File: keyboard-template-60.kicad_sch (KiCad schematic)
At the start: 171 parts

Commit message: Part annotations
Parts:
- removed MX? (x8): MX-NoLED, symbol MX_Alps_Hybrid:MX-NoLED
- added MX? (x8): MX-NoLED, symbol MX_Alps_Hybrid:MX-NoLED
- gave numbers to parts that had none: 163
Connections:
- net COL10: now also MX?.1 (COL)
- net COL11: now also MX?.1 (COL)
- net COL12: now also MX?.1 (COL)
- net COL2: now also MX?.1 (COL)
- net COL3: now also MX?.1 (COL)
- net COL4: now also MX?.1 (COL)
- net COL6: now also MX?.1 (COL)
- net COL8: now also MX?.1 (COL)
- net at D63.2 (A): now also MX?.2 (ROW)
- net at D72.2 (A): now also MX?.2 (ROW)
- net at D37.2 (A): now also MX?.2 (ROW)
- net at D73.2 (A): now also MX?.2 (ROW)
- net at D39.2 (A): now also MX?.2 (ROW)
- net at D65.2 (A): now also MX?.2 (ROW)
- net at D71.2 (A): now also MX?.2 (ROW)
- net at D64.2 (A): now also MX?.2 (ROW)

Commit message: Update annotations
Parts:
- removed MX?: MX-NoLED, symbol MX_Alps_Hybrid:MX-NoLED
- added MX38-2: MX-NoLED, symbol MX_Alps_Hybrid:MX-NoLED
- gave numbers to parts that had none: 7
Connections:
- net COL6: now also MX38-2.1 (COL)
- net at D37.2 (A): now also MX38-2.2 (ROW)
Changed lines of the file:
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@@
   (junction (at 107.95 166.37) (diameter 0) (color 0 0 0 0)
   )
+  (junction (at 133.35 137.16) (diameter 0) (color 0 0 0 0)
+  )
   (junction (at 121.92 147.32) (diameter 0) (color 0 0 0 0)
   )
@@
   (junction (at 64.77 223.52) (diameter 0) (color 0 0 0 0)
   )
-  (junction (at 133.35 137.16) (diameter 0) (color 0 0 0 0)
-  )
   (junction (at 133.35 166.37) (diameter 0) (color 0 0 0 0)
   )
@@
     (stroke (width 0) (type default) (color 0 0 0 0))
   )
+  (wire (pts (xy 133.35 128.27) (xy 133.35 137.16))
+    (stroke (width 0) (type default) (color 0 0 0 0))
+  )
   (wire (pts (xy 294.64 177.8) (xy 304.8 177.8))
     (stroke (width 0) (type default) (color 0 0 0 0))
@@
     (stroke (width 0) (type default) (color 0 0 0 0))
   )
+  (wire (pts (xy 133.35 137.16) (xy 133.35 166.37))
+    (stroke (width 0) (type default) (color 0 0 0 0))
+  )
   (wire (pts (xy 115.57 176.53) (xy 128.27 176.53))
     (stroke (width 0) (type default) (color 0 0 0 0))
@@
     (stroke (width 0) (type default) (color 0 0 0 0))
   )
-  (wire (pts (xy 133.35 137.16) (xy 133.35 166.37))
-    (stroke (width 0) (type default) (color 0 0 0 0))
-  )
   (wire (pts (xy 96.52 223.52) (xy 102.87 223.52))
     (stroke (width 0) (type default) (color 0 0 0 0))
@@
     (stroke (width 0) (type default) (color 0 0 0 0))
   )
-  (wire (pts (xy 133.35 128.27) (xy 133.35 137.16))
-    (stroke (width 0) (type default) (color 0 0 0 0))
-  )
   (wire (pts (xy 171.45 52.07) (xy 171.45 90.17))
     (stroke (width 0) (type default) (color 0 0 0 0))
@@
   (symbol (lib_id "MX_Alps_Hybrid:MX-NoLED") (at 193.04 214.63 0) (unit 1)
     (in_bom yes) (on_board yes) (fields_autoplaced)
-    (property "Reference" "MX?" (id 0) (at 193.9256 208.28 0)
+    (property "Reference" "MX72-2" (id 0) (at 193.9256 208.28 0)
       (effects (font (size 1.524 1.524)))
     )
@@
   (symbol (lib_id "MX_Alps_Hybrid:MX-NoLED") (at 78.74 214.63 0) (unit 1)
     (in_bom yes) (on_board yes) (fields_autoplaced)
-    (property "Reference" "MX?" (id 0) (at 79.6256 208.28 0)
+    (property "Reference" "MX63-2" (id 0) (at 79.6256 208.28 0)
       (effects (font (size 1.524 1.524)))
     )
@@
     (pin "2")
   )
-  (symbol (lib_id "MX_Alps_Hybrid:MX-NoLED") (at 129.54 138.43 0) (unit 1)
-    (in_bom yes) (on_board yes) (fields_autoplaced)
-    (property "Reference" "MX?" (id 0) (at 130.4256 132.08 0)
-      (effects (font (size 1.524 1.524)))
-    )
-    (property "Value" "MX-NoLED" (id 1) (at 130.4256 133.35 0)
-      (effects (font (size 0.508 0.508)))
-    )
-    (property "Footprint" "" (id 2) (at 113.665 139.065 0)
-      (effects (font (size 1.524 1.524)) hide)
-    )
-    (property "Datasheet" "" (id 3) (at 113.665 139.065 0)
-      (effects (font (size 1.524 1.524)) hide)
-    )
-    (pin "1")
-    (pin "2")
-  )
   (symbol (lib_id "MX_Alps_Hybrid:MX-NoLED") (at 104.14 53.34 0) (unit 1)
     (in_bom yes) (on_board yes) (fields_autoplaced)
@@
   (symbol (lib_id "MX_Alps_Hybrid:MX-NoLED") (at 205.74 214.63 0) (unit 1)
     (in_bom yes) (on_board yes) (fields_autoplaced)
-    (property "Reference" "MX?" (id 0) (at 206.6256 208.28 0)
+    (property "Reference" "MX73-2" (id 0) (at 206.6256 208.28 0)
       (effects (font (size 1.524 1.524)))
     )
@@
   (symbol (lib_id "MX_Alps_Hybrid:MX-NoLED") (at 104.14 214.63 0) (unit 1)
     (in_bom yes) (on_board yes) (fields_autoplaced)
-    (property "Reference" "MX?" (id 0) (at 105.0256 208.28 0)
+    (property "Reference" "MX65-2" (id 0) (at 105.0256 208.28 0)
       (effects (font (size 1.524 1.524)))
     )
@@
   (symbol (lib_id "MX_Alps_Hybrid:MX-NoLED") (at 91.44 214.63 0) (unit 1)
     (in_bom yes) (on_board yes) (fields_autoplaced)
-    (property "Reference" "MX?" (id 0) (at 92.3256 208.28 0)
+    (property "Reference" "MX64-2" (id 0) (at 92.3256 208.28 0)
       (effects (font (size 1.524 1.524)))
     )
@@
   (symbol (lib_id "MX_Alps_Hybrid:MX-NoLED") (at 154.94 138.43 0) (unit 1)
     (in_bom yes) (on_board yes) (fields_autoplaced)
-    (property "Reference" "MX?" (id 0) (at 155.8256 132.08 0)
+    (property "Reference" "MX39-2" (id 0) (at 155.8256 132.08 0)
       (effects (font (size 1.524 1.524)))
     )
@@
   (symbol (lib_id "MX_Alps_Hybrid:MX-NoLED") (at 180.34 214.63 0) (unit 1)
     (in_bom yes) (on_board yes) (fields_autoplaced)
-    (property "Reference" "MX?" (id 0) (at 181.2256 208.28 0)
+    (property "Reference" "MX71-2" (id 0) (at 181.2256 208.28 0)
       (effects (font (size 1.524 1.524)))
     )
@@
     (pin "2")
   )
+  (symbol (lib_id "MX_Alps_Hybrid:MX-NoLED") (at 129.54 138.43 0) (unit 1)
+    (in_bom yes) (on_board yes) (fields_autoplaced)
+    (property "Reference" "MX38-2" (id 0) (at 130.4256 132.08 0)
+      (effects (font (size 1.524 1.524)))
+    )
+    (property "Value" "MX-NoLED" (id 1) (at 130.4256 133.35 0)
+      (effects (font (size 0.508 0.508)))
+    )
+    (property "Footprint" "" (id 2) (at 113.665 139.065 0)
+      (effects (font (size 1.524 1.524)) hide)
+    )
+    (property "Datasheet" "" (id 3) (at 113.665 139.065 0)
+      (effects (font (size 1.524 1.524)) hide)
+    )
+    (pin "1")
+    (pin "2")
+  )
   (symbol (lib_id "MX_Alps_Hybrid:MX-NoLED") (at 91.44 129.54 0) (unit 1)
     (in_bom yes) (on_board yes) (fields_autoplaced)
@@
       (reference "MX38") (unit 1) (value "MX-NoLED") (footprint "")
     )
+    (path "/f5c00a1c-6009-46f7-bb45-59e86d627cba"
+      (reference "MX38-2") (unit 1) (value "MX-NoLED") (footprint "")
+    )
     (path "/75294b3a-bcf4-4dee-b1b0-009fd10bd357"
       (reference "MX39") (unit 1) (value "MX-NoLED") (footprint "")
     )
+    (path "/a8b3e0bc-cfe9-4e81-954e-c1b4323435ec"
+      (reference "MX39-2") (unit 1) (value "MX-NoLED") (footprint "")
+    )
     (path "/f1689421-be27-441f-a091-cda9d302f953"
       (reference "MX40") (unit 1) (value "MX-NoLED") (footprint "")
@@
       (reference "MX63") (unit 1) (value "MX-NoLED") (footprint "")
     )
+    (path "/482255ed-4646-4a5e-9984-9a49bd9bd2b6"
+      (reference "MX63-2") (unit 1) (value "MX-NoLED") (footprint "")
+    )
     (path "/257a1eb5-8b33-4e19-9433-ae3ccc490c1b"
       (reference "MX64") (unit 1) (value "MX-NoLED") (footprint "")
     )
+    (path "/a11053e4-9eea-4e3c-beb1-319c66cc54d2"
+      (reference "MX64-2") (unit 1) (value "MX-NoLED") (footprint "")
+    )
     (path "/f2b5c4c7-e8e3-425d-a843-998f7557575d"
       (reference "MX65") (unit 1) (value "MX-NoLED") (footprint "")
     )
+    (path "/9dd9038e-364d-4f87-8675-edd37afc5560"
+      (reference "MX65-2") (unit 1) (value "MX-NoLED") (footprint "")
+    )
     (path "/aa9bb9c5-7107-46ce-943c-1c67b0dac064"
       (reference "MX67") (unit 1) (value "MX-NoLED") (footprint "")
@@
       (reference "MX71") (unit 1) (value "MX-NoLED") (footprint "")
     )
+    (path "/cc00687e-3426-4703-8265-70584ca7426c"
+      (reference "MX71-2") (unit 1) (value "MX-NoLED") (footprint "")
+    )
     (path "/a5e39449-0e3c-481c-85ad-81aa53ee1534"
       (reference "MX72") (unit 1) (value "MX-NoLED") (footprint "")
     )
+    (path "/17ef84ae-2695-4724-93fa-2a883f22ddd9"
+      (reference "MX72-2") (unit 1) (value "MX-NoLED") (footprint "")
+    )
     (path "/7db44cd6-4b9c-480e-9b0e-1b044e3ad474"
       (reference "MX73") (unit 1) (value "MX-NoLED") (footprint "")
     )
+    (path "/8d6e9efb-fed1-4560-b688-d3f05d3f7096"
+      (reference "MX73-2") (unit 1) (value "MX-NoLED") (footprint "")
+    )
     (path "/51589e35-00f2-4091-89f7-be519ee6b00c"
       (reference "MX74") (unit 1) (value "MX-NoLED") (footprint "")
@@
       (reference "MX75") (unit 1) (value "MX-NoLED") (footprint "")
     )
-    (path "/17ef84ae-2695-4724-93fa-2a883f22ddd9"
-      (reference "MX?") (unit 1) (value "MX-NoLED") (footprint "")
-    )
-    (path "/482255ed-4646-4a5e-9984-9a49bd9bd2b6"
-      (reference "MX?") (unit 1) (value "MX-NoLED") (footprint "")
-    )
-    (path "/6bff14b7-7fa8-49c6-9d76-d7cb980abe95"
-      (reference "MX?") (unit 1) (value "MX-NoLED") (footprint "")
-    )
-    (path "/8d6e9efb-fed1-4560-b688-d3f05d3f7096"
-      (reference "MX?") (unit 1) (value "MX-NoLED") (footprint "")
-    )
-    (path "/9dd9038e-364d-4f87-8675-edd37afc5560"
-      (reference "MX?") (unit 1) (value "MX-NoLED") (footprint "")
-    )
-    (path "/a11053e4-9eea-4e3c-beb1-319c66cc54d2"
-      (reference "MX?") (unit 1) (value "MX-NoLED") (footprint "")
-    )
-    (path "/a8b3e0bc-cfe9-4e81-954e-c1b4323435ec"
-      (reference "MX?") (unit 1) (value "MX-NoLED") (footprint "")
-    )
-    (path "/cc00687e-3426-4703-8265-70584ca7426c"
-      (reference "MX?") (unit 1) (value "MX-NoLED") (footprint "")
-    )
     (path "/decb3101-6255-4ab9-8fbc-5a7cad6b1f9e"

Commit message: Add power flag
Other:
- moved on the sheet: C4, C5, C6, C7, C8, F1, J2, R3, R4, R5, R6, U2

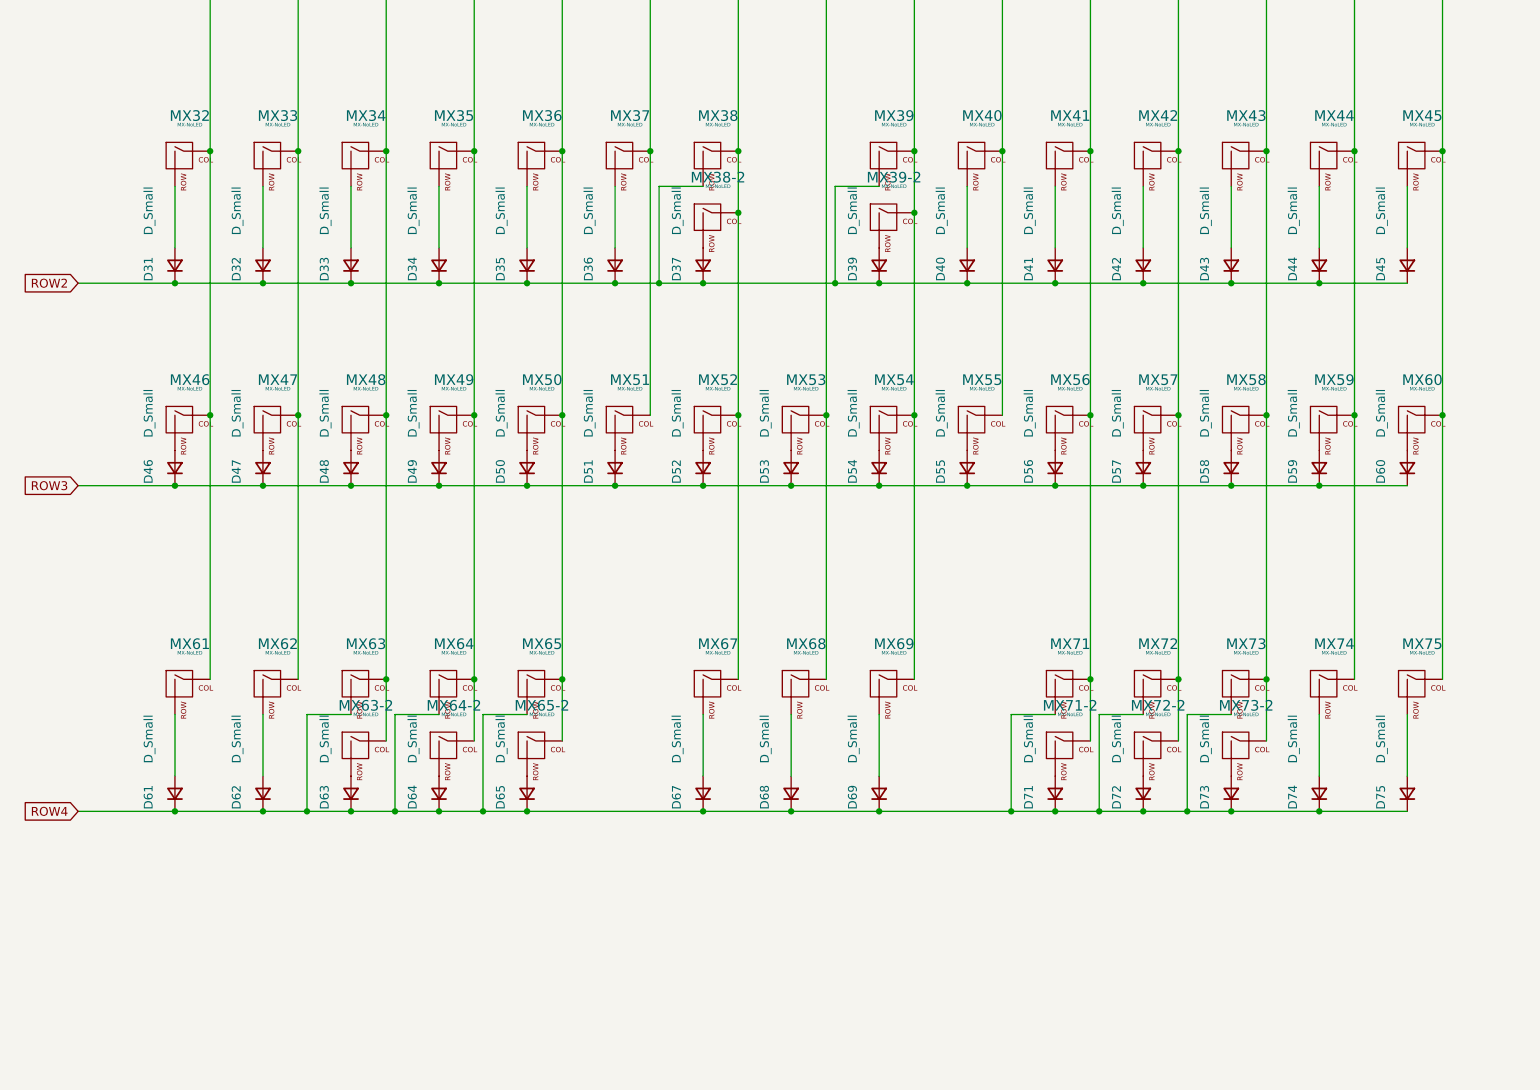
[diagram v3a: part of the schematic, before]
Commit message: Refactor the alternative switch positions
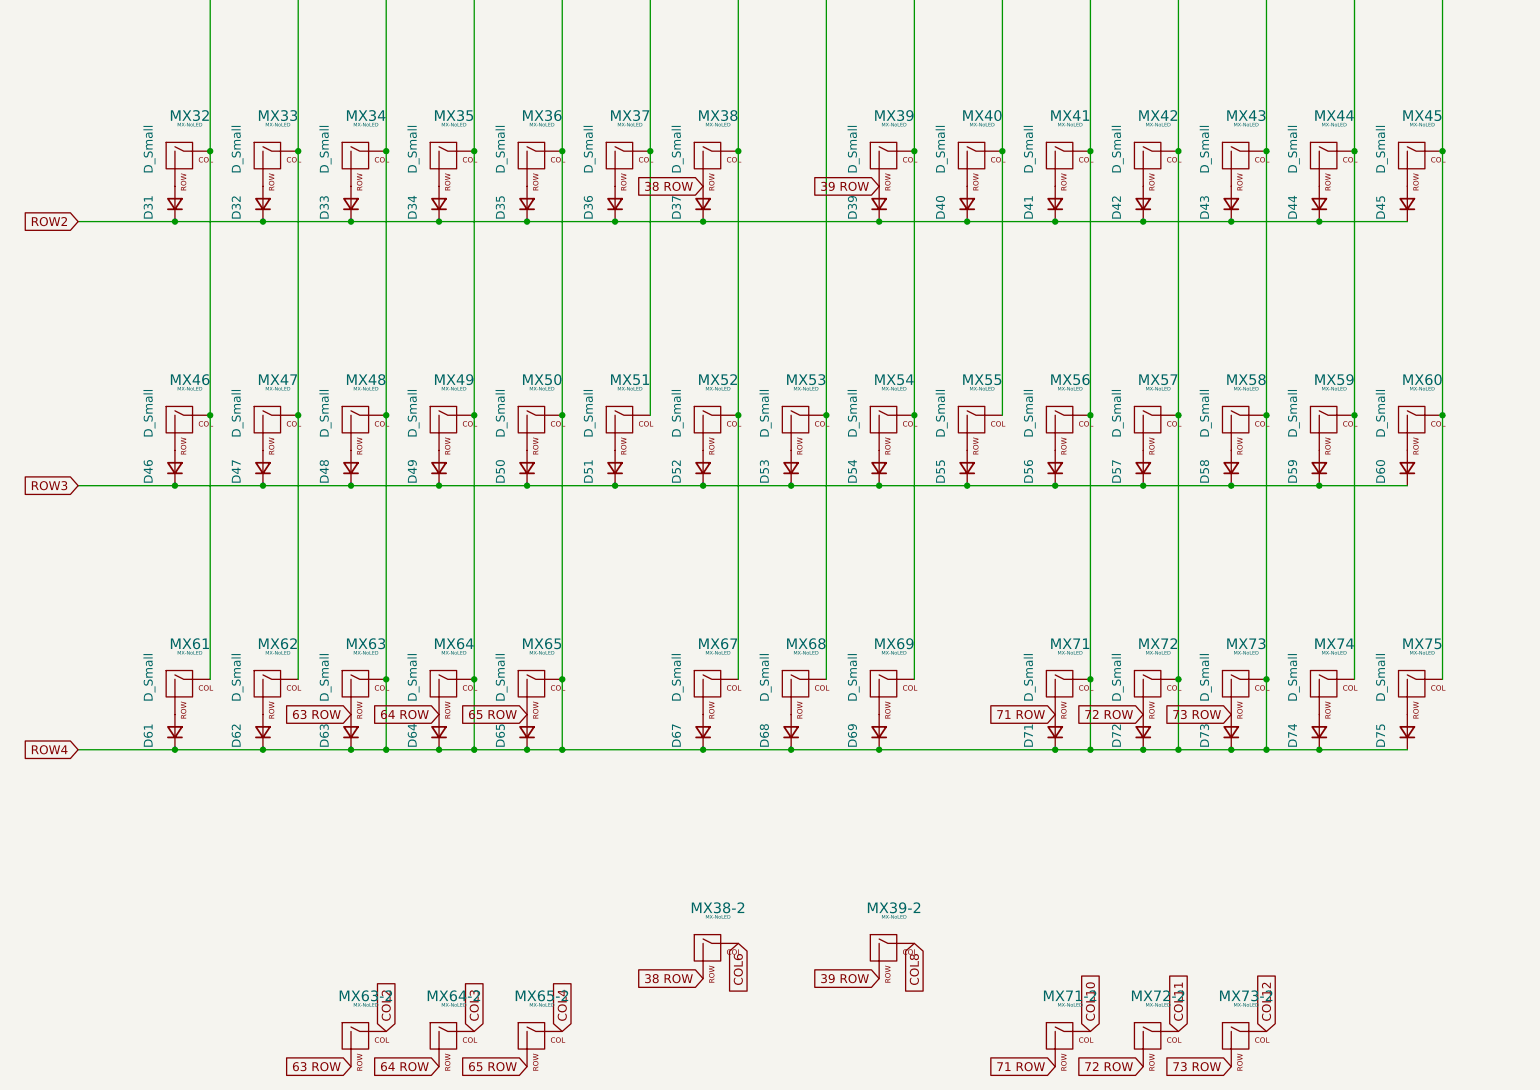
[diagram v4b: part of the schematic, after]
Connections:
- net COL11 is gone; now on net COL10: MX12.1 (COL), MX27.1 (COL), MX42.1 (COL), MX57.1 (COL), MX72-2.1 (COL), MX72.1 (COL), U1.26 (PD6)
- net COL12 is gone; now on net COL10: MX13.1 (COL), MX28.1 (COL), MX43.1 (COL), MX58.1 (COL), MX73-2.1 (COL), MX73.1 (COL), U1.27 (PD7)
- net COL2 is gone; now on net COL10: MX18.1 (COL), MX3.1 (COL), MX34.1 (COL), MX48.1 (COL), MX63-2.1 (COL), MX63.1 (COL), U1.12 (PB7)
- net COL3 is gone; now on net COL10: MX19.1 (COL), MX35.1 (COL), MX4.1 (COL), MX49.1 (COL), MX64-2.1 (COL), MX64.1 (COL), U1.31 (PC6)
- net COL4 is gone; now on net COL10: MX20.1 (COL), MX36.1 (COL), MX5.1 (COL), MX50.1 (COL), MX65-2.1 (COL), MX65.1 (COL), U1.32 (PC7)
- net COL10: now also D61.1 (K), D62.1 (K), D63.1 (K), D64.1 (K), D65.1 (K), D67.1 (K), D68.1 (K), D69.1 (K), D71.1 (K), D72.1 (K), D73.1 (K), D74.1 (K), D75.1 (K), U1.28 (PB4)
- net ROW2: no longer MX38.2 (ROW), MX39.2 (ROW)
- net 72 ROW: now reaches D72.2 (A), MX72-2.2 (ROW)
- net 72 ROW: now also MX72.2 (ROW)
- net 73 ROW: now reaches D73.2 (A), MX73-2.2 (ROW)
- net 73 ROW: now also MX73.2 (ROW)
- net 63 ROW: now reaches D63.2 (A), MX63-2.2 (ROW)
- net 63 ROW: now also MX63.2 (ROW)
- net 65 ROW: now reaches D65.2 (A), MX65-2.2 (ROW)
- net 65 ROW: now also MX65.2 (ROW)
- net 71 ROW: now reaches D71.2 (A), MX71-2.2 (ROW)
- net 71 ROW: now also MX71.2 (ROW)
- net 64 ROW: now reaches D64.2 (A), MX64-2.2 (ROW)
- net 64 ROW: now also MX64.2 (ROW)
- net 39 ROW: now reaches D39.2 (A), MX39-2.2 (ROW)
- net 39 ROW: now also MX39.2 (ROW)
- net 38 ROW: now reaches D37.2 (A), MX38-2.2 (ROW)
- net 38 ROW: now also MX38.2 (ROW)
- removed net ROW4: D61.1 (K), D62.1 (K), D63.1 (K), D64.1 (K), D65.1 (K), D67.1 (K), D68.1 (K), D69.1 (K), D71.1 (K), D72.1 (K), D73.1 (K), D74.1 (K), D75.1 (K), MX63.2 (ROW), MX64.2 (ROW), MX65.2 (ROW), MX71.2 (ROW), MX72.2 (ROW), MX73.2 (ROW), U1.28 (PB4)
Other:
- moved on the sheet: D31, D32, D33, D34, D35, D36, D37, D39, D40, D41, D42, D43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
